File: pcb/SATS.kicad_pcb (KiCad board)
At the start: 2 copper layers, 108.5 x 103.4 mm, 36 parts, among them J1 Raspberry_Pi_2_3, J10 SENSE, J11 SENSE Power, J12 EXT_GPIO, J13 EXT_GPIO, J14 EXT_GPIO, J2 A00-432-262-450, J3 AudioJack4_SwitchTR1, J4 5V, J5 3.3V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

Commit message: Rev 4 - Pretest
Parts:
- removed J14: EXT_GPIO, TerminalConn:PHOENIX_1862042
- removed U4: IRLZ14PBF, Package_TO_SOT_THT:TO-220-3_Horizontal_TabDown
- added Q1: IRLZ14PBF, Package_TO_SOT_THT:TO-220-3_Horizontal_TabDown, F.Cu at (138.2, 60.4)
- R2: value 10 -> 8
- moved C5 98.7 mm to (115.9, 48.4), turned to -90 degrees
- moved L1 95.8 mm to (152.2, 49.7), turned to 90 degrees
- moved R2 94.9 mm to (142.4, 48.6), turned to -90 degrees
- moved D1 80.6 mm to (156.5, 55.9)
- moved J13 30.0 mm to (125.1, 142.5), turned to 180 degrees
- moved J12 28.2 mm to (132.1, 142.5), turned to 180 degrees
- moved J10 23.6 mm to (152.2, 128.6)
- moved J11 23.6 mm to (152.2, 136.4)
- moved J6 23.6 mm to (152.2, 94.6)
- moved J7 23.6 mm to (152.2, 87.6)
- moved J8 23.6 mm to (152.2, 80.6)
- moved J9 23.6 mm to (152.2, 73.6)
- moved SW1 23.6 mm to (152.2, 104.6)
- moved SW2 23.6 mm to (152.2, 111.6)
- moved SW3 23.6 mm to (152.2, 118.6)
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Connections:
- C5 pad 1: +5V -> +12V
- D1 pad 1: +5V -> +12V
- J1 pad 10: Wiegand 0 -> Card Beeper
- J1 pad 12: Wiegand 1 -> Wiegand 0
- J1 pad 16: Card RED -> Wiegand 1
- J1 pad 18: Card GRN -> Card RED
- J1 pad 19: LED Sig2 -> LED SIG
- J1 pad 21: LED Sig4 -> LED EN2
- J1 pad 22: Latch -> Card GRN
- J1 pad 23: LED Sig1 -> LED EN4
- J1 pad 27: LED Sig3 -> LED EN1
- J1 pad 29: TOUCH -> LED EN3
- J1 pad 31: PHOTO -> 1-Wire
- J1 pad 32: EXT_GPIO12 -> TOUCH
- J1 pad 33: EXT_GPIO13 -> unconnected-(J1-PWM1/GPIO13-Pad33)
- J1 pad 36: EXT_GPIO16 -> PHOTO
- J1 pad 37: 1-Wire -> EXT_GPIO26
- J1 pad 8: Card Beeper -> Latch
- J11 pad 1: Earth -> +5V
- J11 pad 2: Earth -> +5V
- J11 pad 3: +5V -> Earth
- J11 pad 4: +5V -> Earth
- J12 pad 1: EXT_GPIO12 -> EXT_GPIO20
- J12 pad 2: EXT_GPIO12 -> EXT_GPIO20
- J12 pad 3: EXT_GPIO13 -> EXT_GPIO21
- J12 pad 4: EXT_GPIO13 -> EXT_GPIO21
- J13 pad 1: EXT_GPIO16 -> EXT_GPIO26
- J13 pad 2: EXT_GPIO16 -> EXT_GPIO26
- J4 pad 1: +5V -> +12V
- J4 pad 2: +5V -> +12V
- J4 pad 3: Earth -> +5V
- J4 pad 4: Earth -> +5V
- L1 pad 1: +5V -> Net-(L1-1-Pad2)
- L1 pad 2: +5V -> Net-(L1-1-Pad2)
- L1 pad 3: Net-(L1-2-Pad3) -> +12V
- L1 pad 4: Net-(L1-2-Pad3) -> +12V
- R2 pad 1: Net-(L1-2-Pad3) -> Net-(L1-1-Pad2)
- U3 pad 10: LED Sig2 -> LED SIG
- U3 pad 14: LED Sig1 -> LED SIG
- U3 pad 15: +3V3 -> LED EN1
- U3 pad 2: +3V3 -> LED EN3
- U3 pad 3: LED Sig3 -> LED SIG
- U3 pad 6: LED Sig4 -> LED SIG
- U3 pad 7: +3V3 -> LED EN4
- U3 pad 9: +3V3 -> LED EN2
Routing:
- net LED Sig1: track 106.1 -> 0.00 mm
- net LED SIG: track 0.00 -> 105.7 mm
- net LED EN1: track 0.00 -> 105.0 mm
- net LED Sig2: track 101.8 -> 0.00 mm
- net LED EN3: track 0.00 -> 97.3 mm
- net LED Sig3: track 97.0 -> 0.00 mm
- net LED EN2: track 0.00 -> 95.3 mm
- net LED Sig4: track 94.6 -> 0.00 mm
- net LED EN4: track 0.00 -> 88.8 mm
- net +12V: track 0.00 -> 55.7 mm
- net Latch: track 56.3 -> 13.4 mm
- net EXT_GPIO13: track 41.8 -> 0.00 mm
- net EXT_GPIO12: track 39.3 -> 0.00 mm
- net EXT_GPIO16: track 38.5 -> 0.00 mm
- net EXT_GPIO26: track 0.00 -> 38.1 mm
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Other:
- board text added: "12V"
- board text added: "8"
- board text added: "IO26"
- board text added: "SATS PCB REV 4 - MATTHEW HAAHR & ALEXANDER HAYDEN MAY 2023 WPI LENS & LIGHTS"
- board text removed: "10"
- board text removed: "IO12"
- board text removed: "IO13"
- board text removed: "IO16"
- board text removed: "SATS PCB REV 3 - MATTHEW HAAHR & ALEXANDER HAYDEN APRIL 2023 WPI LENS & LIGHTS"

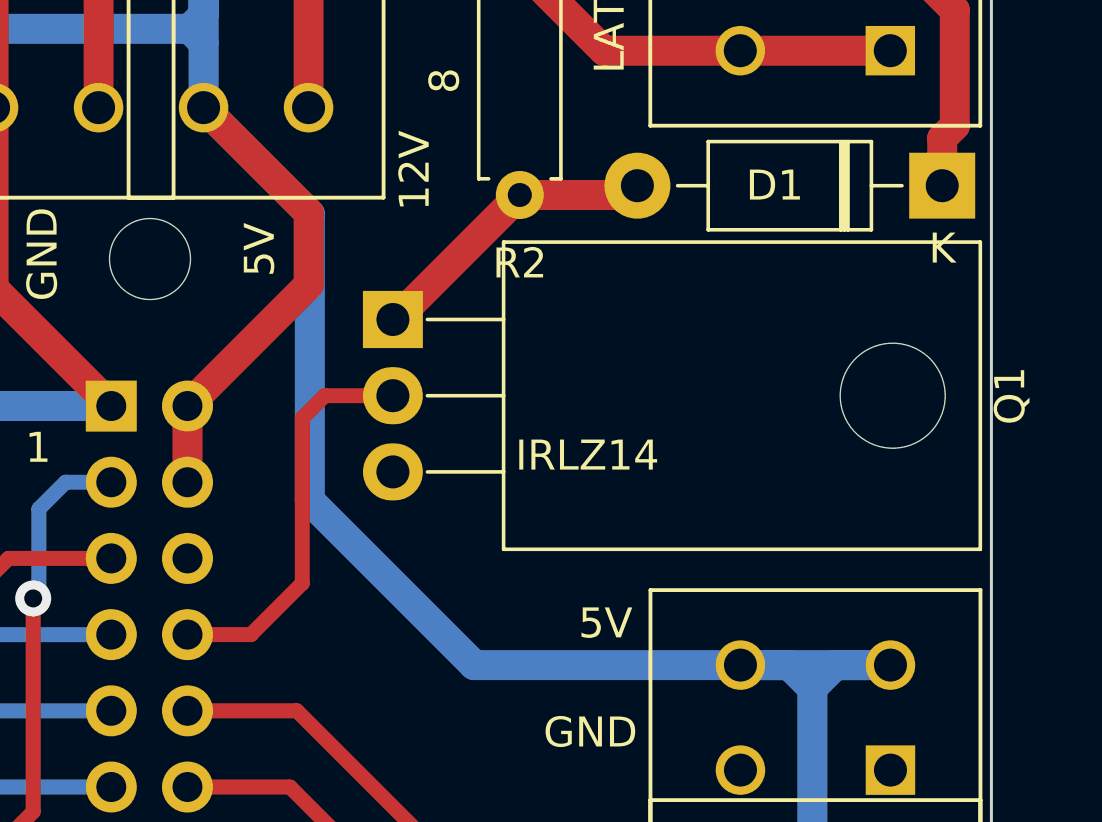
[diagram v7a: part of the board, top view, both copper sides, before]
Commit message: Fix MOSFET
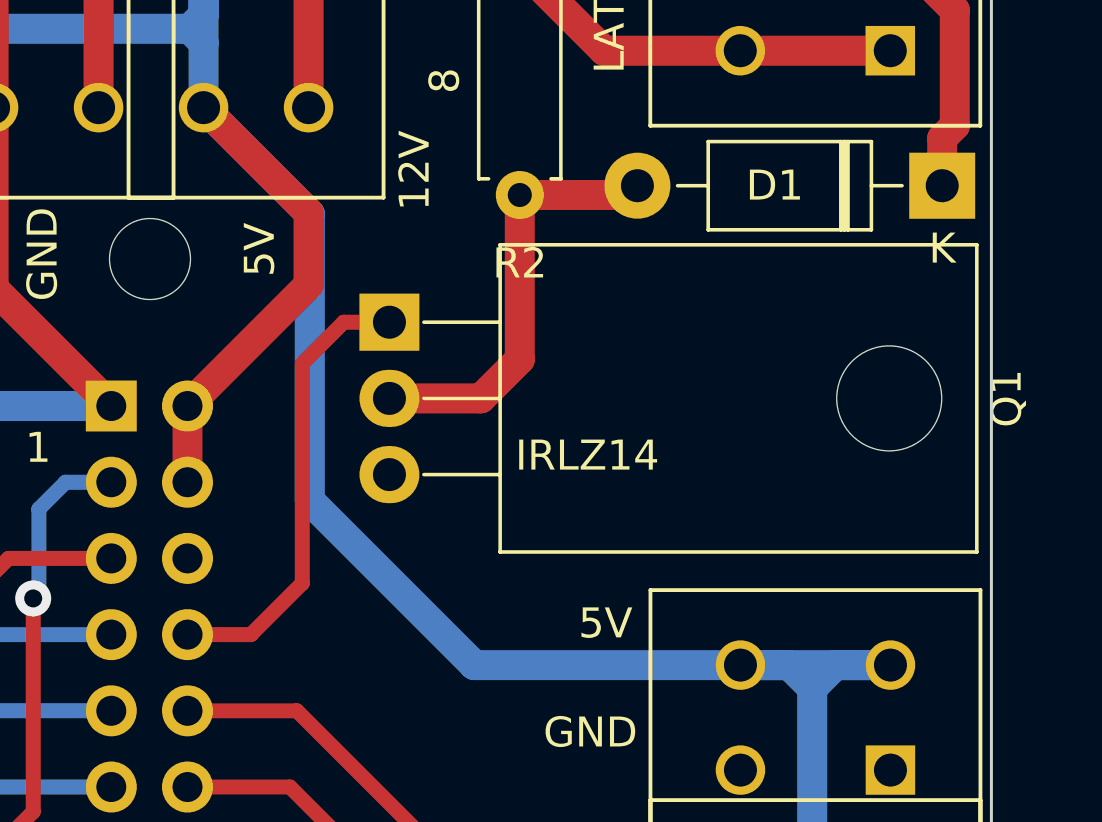
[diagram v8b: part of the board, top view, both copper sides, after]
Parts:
- moved Q1 0.15 mm to (138.0, 60.5)
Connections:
- Q1 pad 1: Net-(D1-A) -> Latch
- Q1 pad 2: Latch -> Net-(D1-A)
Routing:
- net Net-(D1-A): track 10.00 -> 14.4 mm
- net Latch: track 13.4 -> 15.3 mm
